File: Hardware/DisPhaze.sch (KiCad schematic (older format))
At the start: 78 parts, among them J3 Conn_01x04_Male, U1 STM32F405RGTx, Y1 Crystal

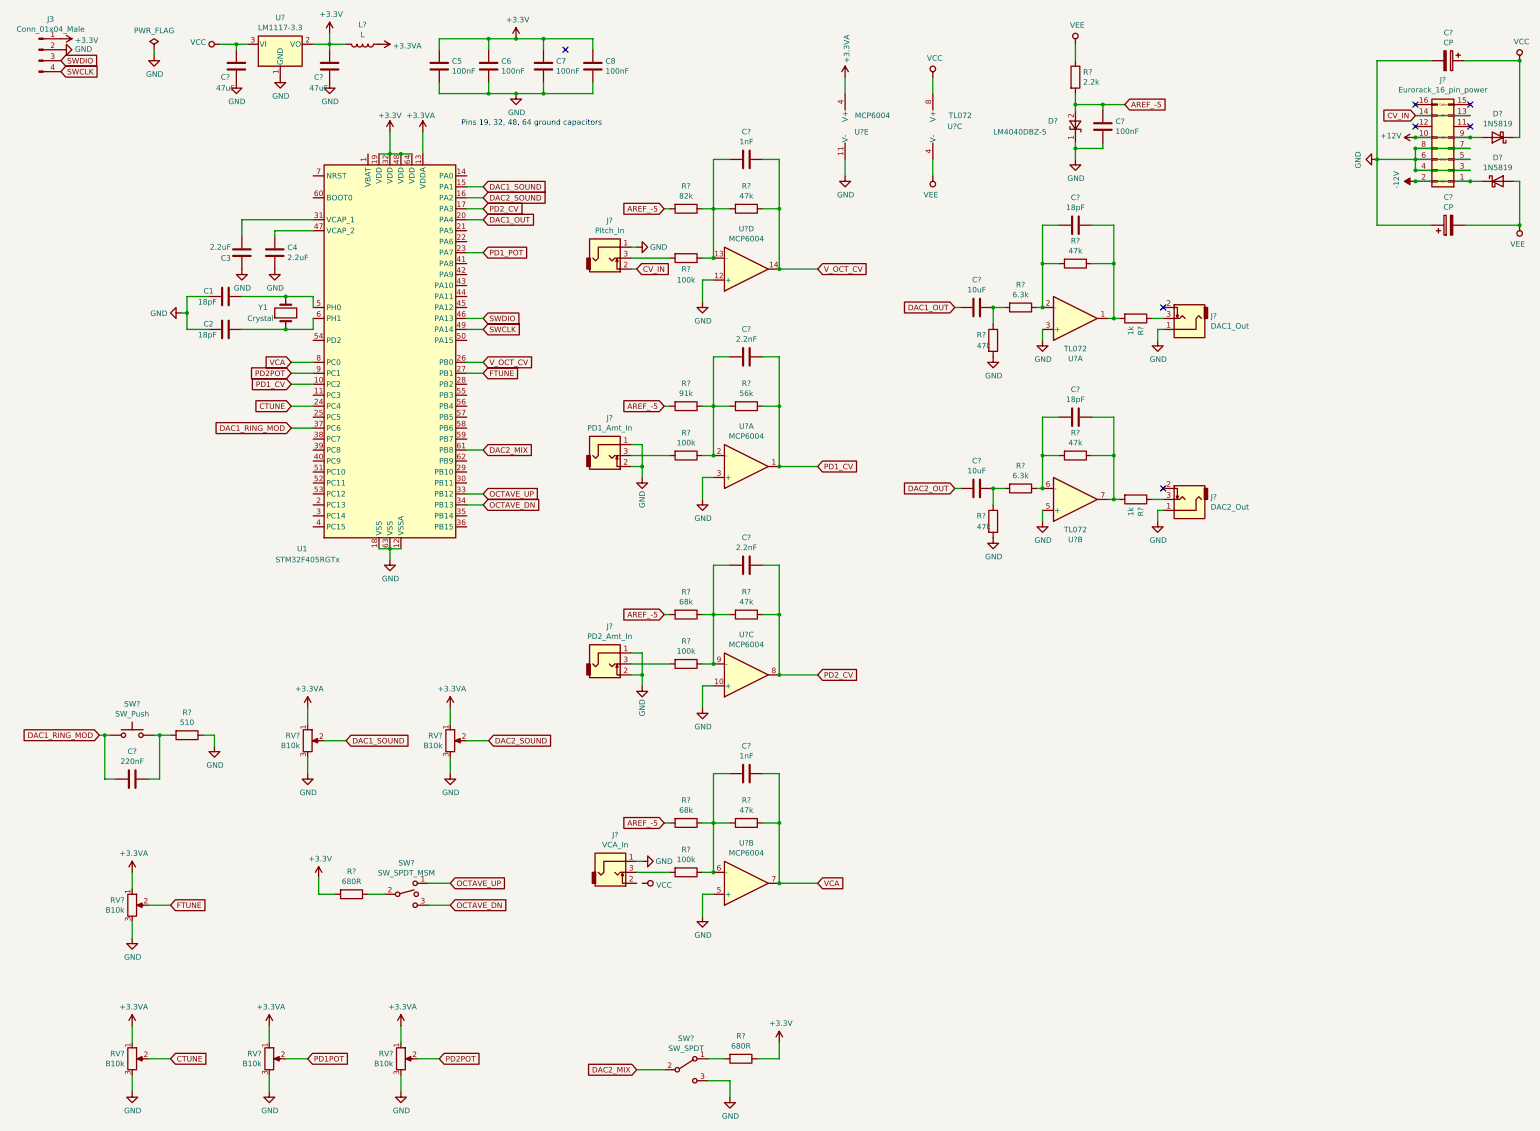
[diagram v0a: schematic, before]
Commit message: Schematic tidied up and command prefetch enabled
Prefetch seems to have caused issues for some revisions but tested fine with revision Y and performance improvements seen
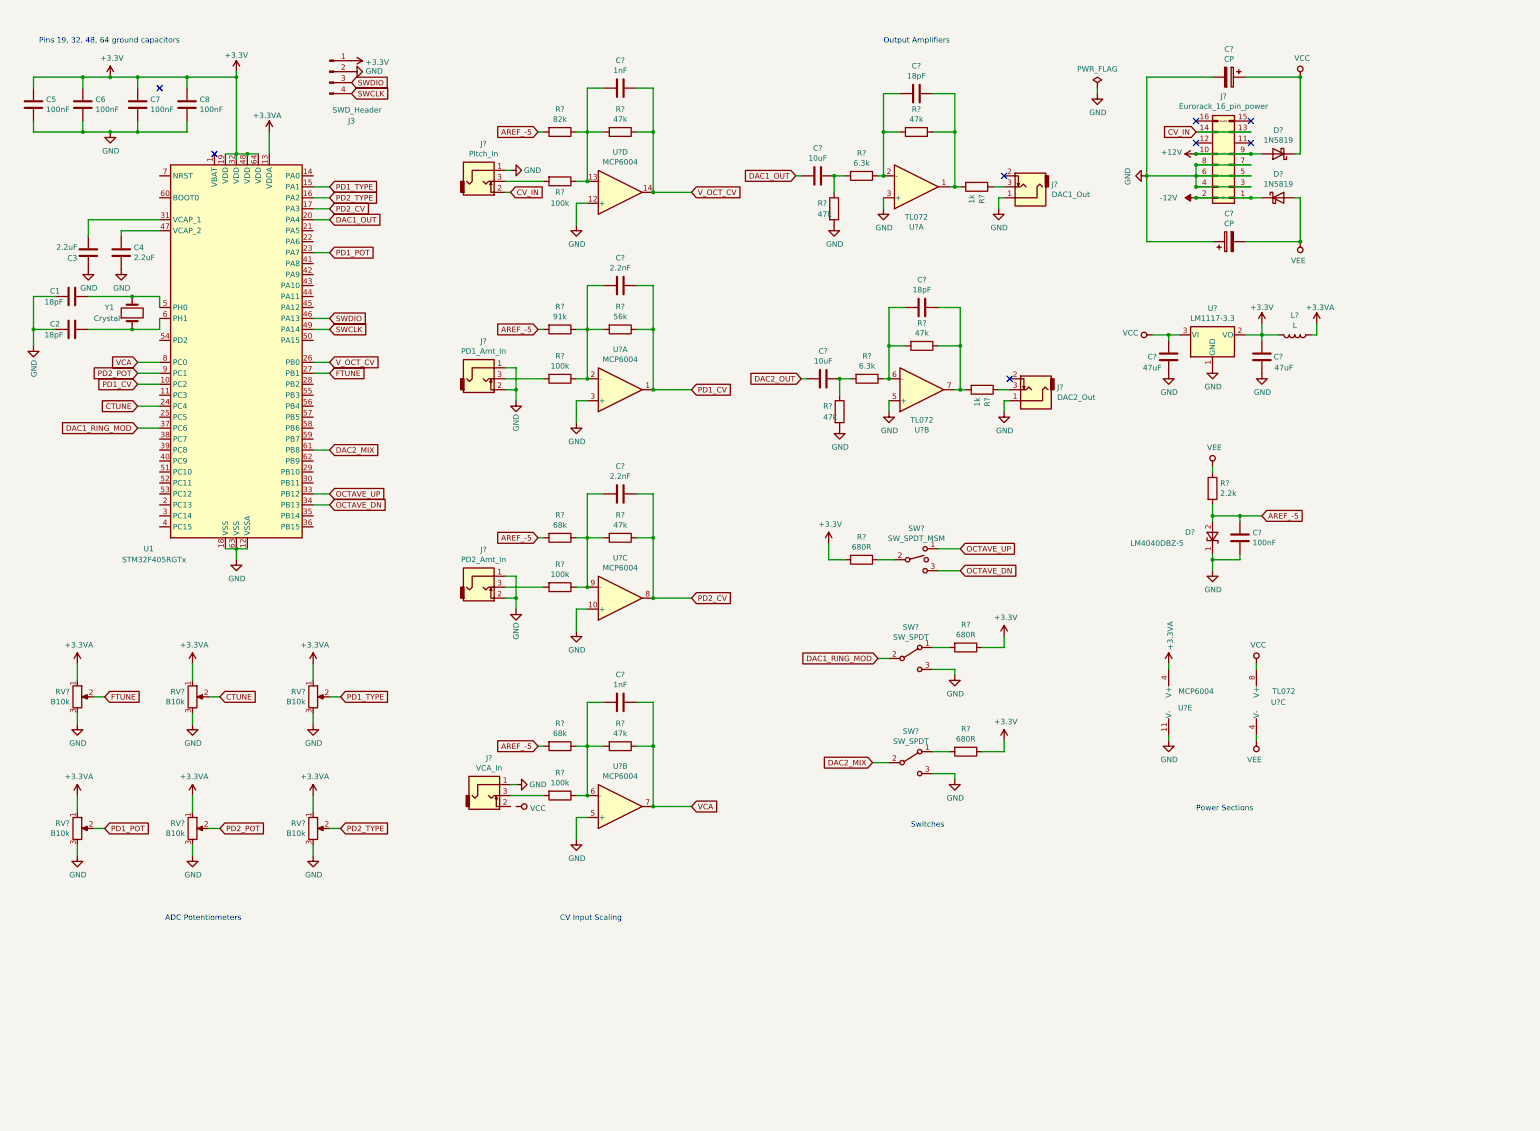
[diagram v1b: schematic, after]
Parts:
- removed C?: 220nF, symbol Device:C
- removed R?: 510, symbol Device:R
- removed SW?: SW_Push, symbol Switch:SW_Push
- added R?: 680R, symbol Device:R
- added SW?: SW_SPDT, symbol Switch:SW_SPDT
- J3: value Conn_01x04_Male -> SWD_Header
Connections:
- net PD1POT is gone; now on net PD1_POT: RV?.2
- net +3V3: now also R?.1
- net DAC1_RING_MOD: now also SW?.2 (B)
- net GND: now also SW?.3 (C)
- net DAC1_SOUND renamed PD1_TYPE
- net DAC2_SOUND renamed PD2_TYPE
- net PD2POT renamed PD2_POT
- new net: R?.2, SW?.1 (A)
- no-connect marks 7 -> 8
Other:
- note added: "ADC Potentiometers"
- note added: "CV Input Scaling"
- note added: "Output Amplifiers"
- note added: "Power Sections"
- note added: "Switches"
- moved on the sheet: C1, C2, C3, C4, C5, C6, C7, C8, C?, D?, J3, J?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

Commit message: Tweaks to output amplifier and VCA normal
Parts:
- added R?: 47k, symbol Device:R
- R? (x2): value 47k -> 68k
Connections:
- net VCC: now also R?.1
- net at J?.2: now also R?.2
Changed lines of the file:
@@
 P 8800 3550
 F 0 "R?" V 8593 3550 50  0000 C CNN
-F 1 "47k" V 8684 3550 50  0000 C CNN
+F 1 "68k" V 8684 3550 50  0000 C CNN
 F 2 "" V 8730 3550 50  0001 C CNN
 F 3 "~" H 8800 3550 50  0001 C CNN
@@
 P 8750 1600
 F 0 "R?" V 8543 1600 50  0000 C CNN
-F 1 "47k" V 8634 1600 50  0000 C CNN
+F 1 "68k" V 8634 1600 50  0000 C CNN
 F 2 "" V 8680 1600 50  0001 C CNN
 F 3 "~" H 8750 1600 50  0001 C CNN
@@
 L power:VCC #PWR0152
 U 1 1 5CC588A1
-P 5100 7750
-F 0 "#PWR0152" H 5100 7600 50  0001 C CNN
-F 1 "VCC" V 5117 7878 50  0000 L CNN
-F 2 "" H 5100 7750 50  0001 C CNN
-F 3 "" H 5100 7750 50  0001 C CNN
-	1    5100 7750
-	0    1    1    0
+P 5100 8150
+F 0 "#PWR0152" H 5100 8000 50  0001 C CNN
+F 1 "VCC" V 5117 8278 50  0000 L CNN
+F 2 "" H 5100 8150 50  0001 C CNN
+F 3 "" H 5100 8150 50  0001 C CNN
+	1    5100 8150
+	-1   0    0    1
 $EndComp
 $Comp
@@
 Text Notes 8700 7950 0    50   ~ 0
 Switches
+$Comp
+L Device:R R?
+U 1 1 5CFC5EAE
+P 5100 7950
+F 0 "R?" V 4893 7950 50  0000 C CNN
+F 1 "47k" V 4984 7950 50  0000 C CNN
+F 2 "" V 5030 7950 50  0001 C CNN
+F 3 "~" H 5100 7950 50  0001 C CNN
+	1    5100 7950
+	-1   0    0    1
+$EndComp
+Wire Wire Line
+	5050 7750 5100 7750
+Wire Wire Line
+	5100 7750 5100 7800
+Wire Wire Line
+	5100 8100 5100 8150
 $EndSCHEMATC

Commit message: Start PCB layout
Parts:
- added C11, C12, C6, C7: 100nF, Capacitors_SMD:C_0805_HandSoldering, symbol Device:C
- C13, C14, C15, C16, C17, C18, C19, C20, C24: renamed from C?; footprint (none) -> Capacitors_SMD:C_0805_HandSoldering
- C21, C25: renamed from C?; footprint (none) -> Capacitors_SMD:CP_Elec_5x5.8
- C22, C23: renamed from C?; value CP -> 22uF; footprint (none) -> Capacitors_SMD:CP_Elec_4x5.8
- CTune1, FTune1, PD1Amt1, PD1Type1, PD2Amt1, PD2Type1: renamed from RV?; footprint (none) -> Potentiometers:Potentiometer_Alps_RK09K_Horizontal
- D1: renamed from D?; footprint Package_TO_SOT_SMD:SOT-23 -> TO_SOT_Packages_SMD:SOT-23
- D2, D3: renamed from D?; footprint Diode_THT:D_DO-41_SOD81_P10.16mm_Horizontal -> Diodes_SMD:D_SOD-123
- J1: renamed from J3; footprint Connectors_Multicomp:Multicomp_MC9A12-1034_2x05x2.54mm_Straight -> Custom_Footprints:4pin_header
- J2, J3, J4, J5, J6, J7: renamed from J?; footprint (none) -> Custom_Footprints:THONKICONN_hole
- J8: renamed from J?; footprint (none) -> Custom_Footprints:Eurorack_16_pin_header
- L1: renamed from L?; footprint (none) -> Resistors_SMD:R_0805_HandSoldering
- R1, R10, R11, R12, R13, R14, R15, R16, R17, R18, R19, R2, R20, R21, R22, R23, R24, R25, R3, R4, R5, R6, R7, R8, R9: renamed from R?; footprint (none) -> Resistors_SMD:R_0805_HandSoldering
- SW1: renamed from SW?; value SW_SPDT -> DAC1_RingMod_Switch; footprint (none) -> Custom_Footprints:SPDTSubMiniature
- SW2: renamed from SW?; value SW_SPDT -> DAC2_Mix_Switch; footprint (none) -> Custom_Footprints:SPDTSubMiniature
- SW3: renamed from SW?; value SW_SPDT_MSM -> Octave_Switch; footprint (none) -> Custom_Footprints:SPDTSubMiniature
- U2: renamed from U?; footprint (none) -> SMD_Packages:SOIC-14_N
- U3: renamed from U?; footprint (none) -> SMD_Packages:SOIC-8-N
- U4: renamed from U?; footprint (none) -> TO_SOT_Packages_SMD:SOT-223
- renumbered C5 to C1, C8 to C10, C1 to C2, C2 to C3, C6 to C4, C3 to C5, C4 to C8, C7 to C9
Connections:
- net CTUNE: now also U1.27 (PB1); no longer U1.24 (PC4)
- net DAC2_OUT: now also U1.21 (PA5)
- net FTUNE: now also U1.24 (PC4), C6.1; no longer U1.27 (PB1)
- net GND: now also U2.12 (+), U2.5 (+), C11.2, C12.2, C6.2, C7.2; no longer U2.12 (+), U2.5 (+)
- net OCTAVE_DN: no longer U1.34 (PB13)
- net OCTAVE_UP: no longer U1.33 (PB12)
- net PD1_POT: now also C7.1
- net PD1_TYPE: now also C12.1
- net PD2_POT: now also C11.1
- net VCA: now also U2.14; no longer U2.7
- net V_OCT_CV: now also U2.7; no longer U2.14
- net at C13.1, R10.2, R2.1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: now also U2.6 (-); no longer U2.13 (-)
- net at C16.1, R13.2, R8.1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: now also U2.13 (-); no longer U2.6 (-)
- no-connect marks 8 -> 40

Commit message: Tweaks to pcb layout v1
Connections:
- net OCTAVE_DN: now also U1.53 (PC12)
- net OCTAVE_UP: now also U1.51 (PC10)
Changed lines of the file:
@@
 Wire Wire Line
 	8950 5600 9150 5600
-Text GLabel 3400 4400 2    50   Input ~ 0
+Text GLabel 1650 4700 0    50   Input ~ 0
 OCTAVE_UP
-Text GLabel 3400 4200 2    50   Input ~ 0
+Text GLabel 1650 4900 0    50   Input ~ 0
 OCTAVE_DN
-Wire Wire Line
-	3250 5000 3400 5000
-Wire Wire Line
-	3250 4900 3400 4900
 $Comp
 L Amplifier_Operational:TL072 U3
@@
 NoConn ~ 1850 4500
 NoConn ~ 1850 4600
-NoConn ~ 1850 4700
 NoConn ~ 1850 4800
-NoConn ~ 1850 4900
 NoConn ~ 1850 5000
 NoConn ~ 1850 5100
@@
 Wire Wire Line
 	9850 1200 9850 1250
+Wire Wire Line
+	1650 4900 1850 4900
+Wire Wire Line
+	1650 4700 1850 4700
+NoConn ~ 3250 5000
+NoConn ~ 3250 4900
 $EndSCHEMATC

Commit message: Updated GitIgnore
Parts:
- J1: footprint Custom_Footprints:4pin_header -> Custom_Footprints:SWD_header
- U4: footprint TO_SOT_Packages_SMD:SOT-223 -> TO_SOT_Packages_SMD:TO-252-3_TabPin2
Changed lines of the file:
@@
 F 0 "J1" H 3600 600 50  0000 C CNN
 F 1 "SWD_Header" H 3650 700 50  0000 C CNN
-F 2 "Custom_Footprints:4pin_header" H 3400 1050 50  0001 C CNN
+F 2 "Custom_Footprints:SWD_header" H 3400 1050 50  0001 C CNN
 F 3 "~" H 3400 1050 50  0001 C CNN
 	1    3400 1050
@@
 F 0 "U4" H 11450 3692 50  0000 C CNN
 F 1 "LM1117-3.3" H 11450 3601 50  0000 C CNN
-F 2 "TO_SOT_Packages_SMD:SOT-223" H 11450 3450 50  0001 C CNN
+F 2 "TO_SOT_Packages_SMD:TO-252-3_TabPin2" H 11450 3450 50  0001 C CNN
 F 3 "http://www.ti.com/lit/ds/symlink/lm1117.pdf" H 11450 3450 50  0001 C CNN
 	1    11450 3450

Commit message: Panel outline first draft
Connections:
- net OCTAVE_DN: now also SW3.1; no longer SW3.3
- net OCTAVE_UP: now also SW3.3; no longer SW3.1
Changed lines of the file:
@@
 Wire Wire Line
 	7950 5500 8100 5500
+Text GLabel 9150 5600 2    50   Input ~ 0
+OCTAVE_UP
 Text GLabel 9150 5400 2    50   Input ~ 0
-OCTAVE_UP
-Text GLabel 9150 5600 2    50   Input ~ 0
 OCTAVE_DN
 Wire Wire Line
